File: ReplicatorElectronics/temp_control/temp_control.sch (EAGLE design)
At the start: 4 parts, among them Q1 IRL640A

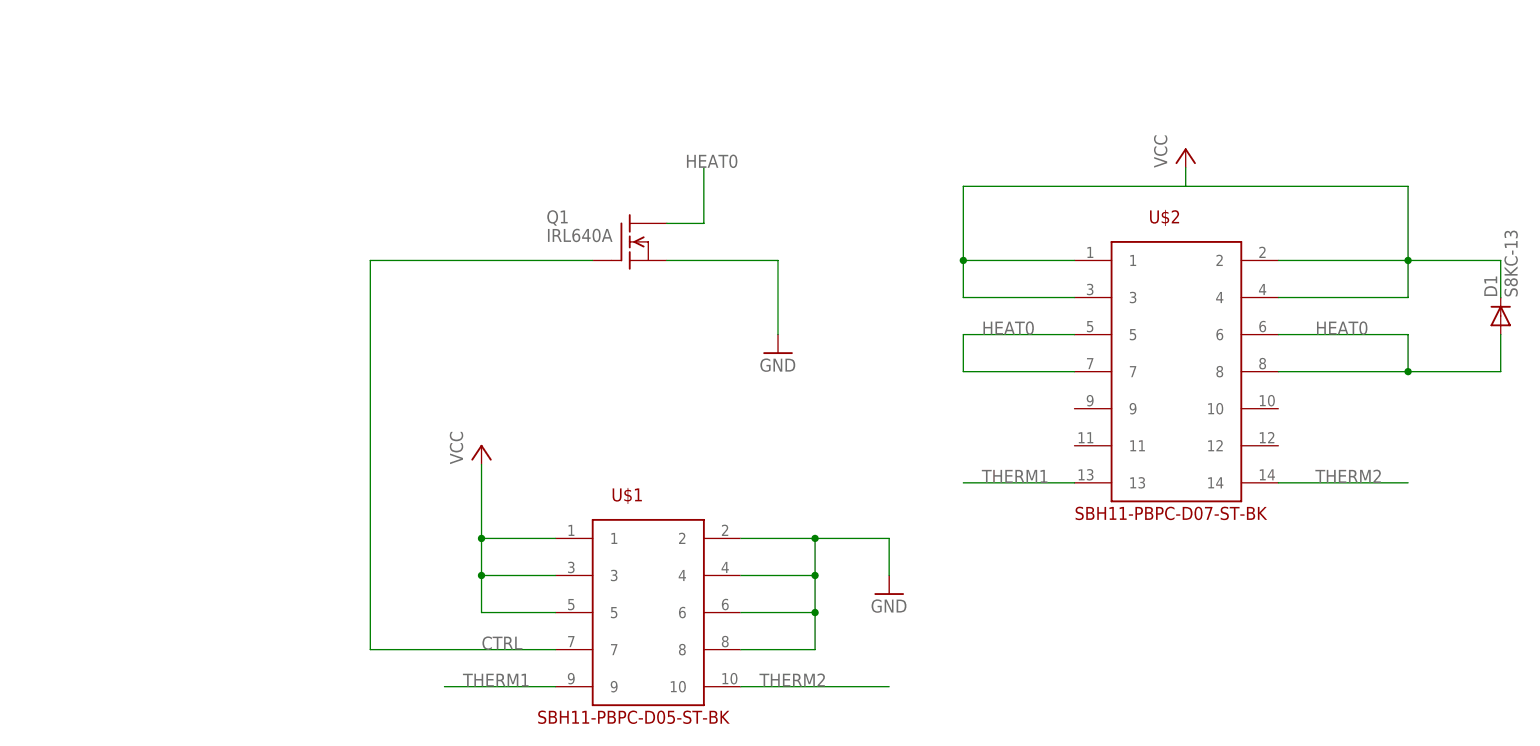
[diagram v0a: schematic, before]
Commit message: 3/17/12: Rev. 02 Temp Control Board. Replaced 2x7 rectangular header with 0.100" pitch screw terminal, added high-side totem pole driver for MOSFET, added clearance holes for mounting screws. Swapped diode D1 for slightly smaller part.
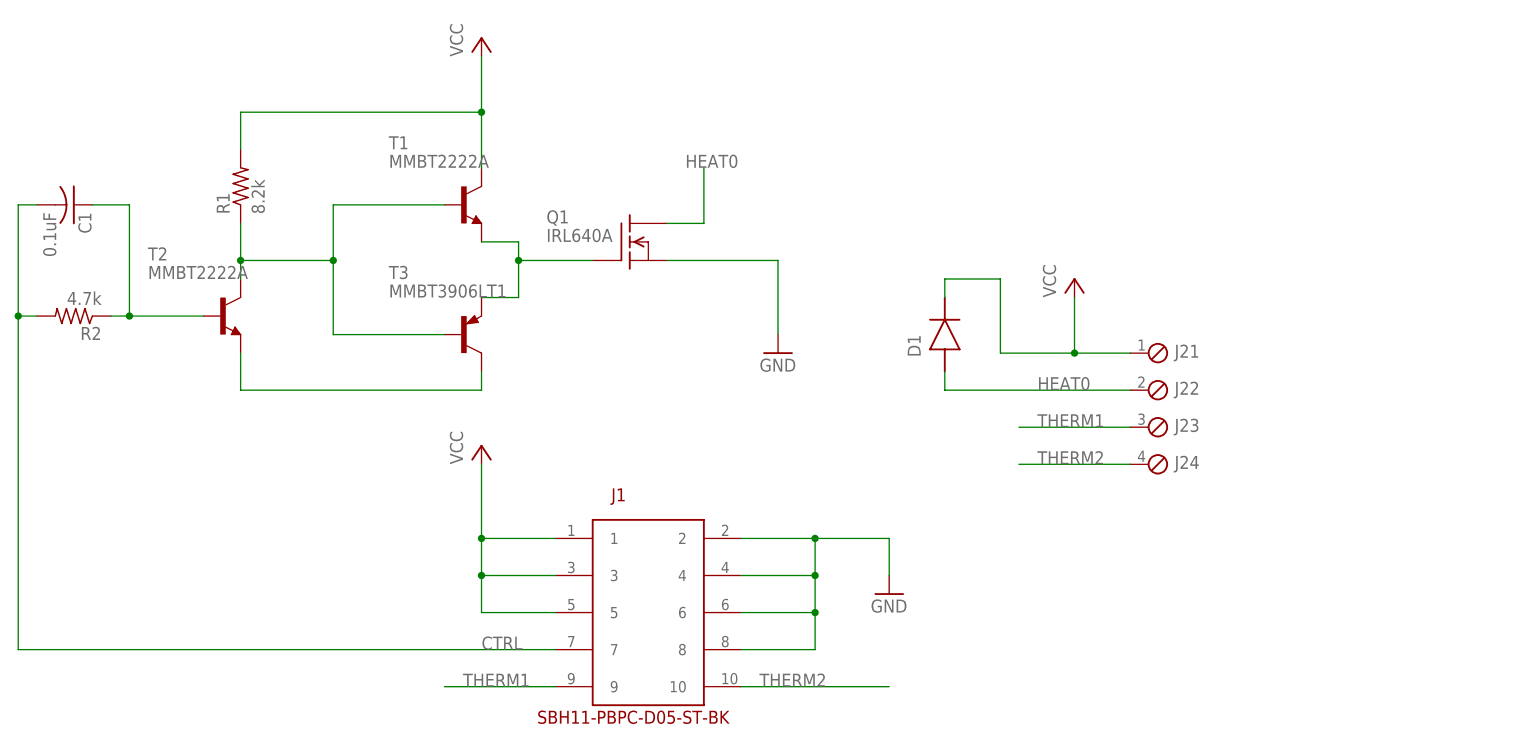
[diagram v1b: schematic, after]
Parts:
- removed U$2: SBH11-PBPC-D07-ST-BK, SBH11-PBPC-D07-ST-BK:SBH11-PBPC-D07-ST-BK
- added C1: 0.1uF, resistor:C-USC0603
- added J2: OSTVN04A150, con-OST-254:OSTVN04A150
- added R1: 8.2k, resistor:R-US_R0603
- added R2: 4.7k, resistor:R-US_R0603
- added T1, T2: MMBT2222A, transistor:MMBT2222ALT1-NPN-SOT23-BEC
- added T3: MMBT3906LT1, transistor:MMBT3906LT1-PNP-SOT23-BEC
- D1: value S8KC-13 -> B340A-13-F; device diode:DIODE-SMC -> chipKIT_Max32:DISCRETE_DIODESMA
- renumbered U$1 to J1
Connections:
- new net N$3: C1.1, R2.1, T2.B
- new net N$4: R1.1, T1.B, T2.C, T3.B
- new net N$6: Q1.G, T1.E, T3.E
- new net N$8: T2.E, T3.C
- net CTRL: now also C1.2, R2.2; no longer Q1.G
- net HEAT0: now also J22.1; no longer U$2.5, U$2.6, U$2.7, U$2.8
- net THERM1: now also J23.1; no longer U$2.13
- net THERM2: now also J24.1; no longer U$2.14
- net VCC: now also J21.1, R1.2, T1.C; no longer U$2.1, U$2.2, U$2.3, U$2.4

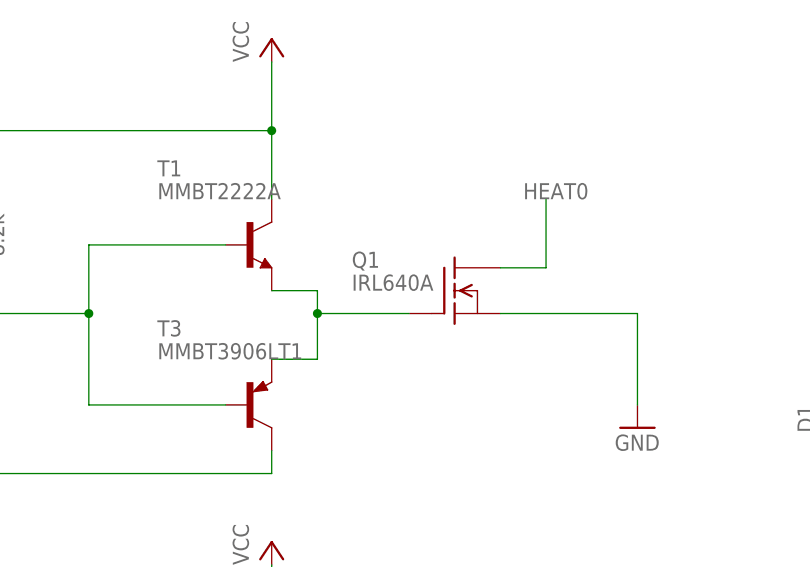
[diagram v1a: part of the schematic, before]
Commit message: 3/31/12: Rev. 3 of temp control board. Modified 2x5 header symbol, generated DXF files (one with holes only, another with holes and high-profile parts).
~ 0.5 hrs invested.
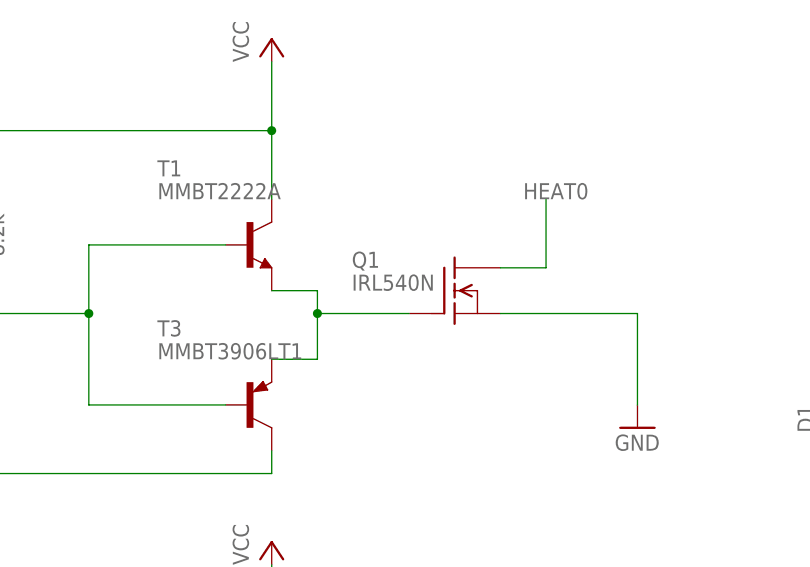
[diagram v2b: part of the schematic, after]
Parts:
- Q1: value IRL640A -> IRL540N
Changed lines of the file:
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@@
 </classes>
 <parts>
-<part name="Q1" library="transistor-fet" deviceset="SUP75N06-08" device="" value="IRL640A"/>
-<part name="J1" library="SBH11-PBPC-D05-ST-BK" deviceset="SBH11-PBPC-D05-ST-BK" device=""/>
+<part name="Q1" library="transistor-fet" deviceset="SUP75N06-08" device="" value="IRL540N"/>
 <part name="P+1" library="supply1" deviceset="VCC" device=""/>
 <part name="GND1" library="supply1" deviceset="GND" device=""/>
@@
 <part name="FRAME1" library="frames" deviceset="FRAME_C_L" device=""/>
 <part name="D1" library="chipKIT_Max32" deviceset="DISCRETE_DIODE" device="SMA" value="B340A-13-F"/>
+<part name="J1" library="SBH11-PBPC-D05-ST-BK" deviceset="SBH11-PBPC-D05-ST-BK" device=""/>
 </parts>
 <sheets>
@@
 <instances>
 <instance part="Q1" gate="G$1" x="22.86" y="73.66"/>
-<instance part="J1" gate="G$1" x="22.86" y="22.86"/>
 <instance part="P+1" gate="VCC" x="2.54" y="45.72"/>
 <instance part="GND1" gate="1" x="58.42" y="25.4"/>
@@
 <instance part="FRAME1" gate="G$2" x="200.66" y="-160.02"/>
 <instance part="D1" gate="G$1" x="66.04" y="60.96" rot="R270"/>
+<instance part="J1" gate="G$1" x="22.86" y="22.86"/>
 </instances>
 <busses>
@@
 <net name="VCC" class="0">
 <segment>
-<pinref part="J1" gate="G$1" pin="5"/>
 <wire x1="12.7" y1="22.86" x2="2.54" y2="22.86" width="0.1524" layer="91"/>
 <wire x1="2.54" y1="22.86" x2="2.54" y2="27.94" width="0.1524" layer="91"/>
-<pinref part="J1" gate="G$1" pin="3"/>
 <wire x1="2.54" y1="27.94" x2="12.7" y2="27.94" width="0.1524" layer="91"/>
 <wire x1="2.54" y1="27.94" x2="2.54" y2="33.02" width="0.1524" layer="91"/>
 <junction x="2.54" y="27.94"/>
-<pinref part="J1" gate="G$1" pin="1"/>
 <wire x1="2.54" y1="33.02" x2="12.7" y2="33.02" width="0.1524" layer="91"/>
 <wire x1="2.54" y1="33.02" x2="2.54" y2="43.18" width="0.1524" layer="91"/>
 <junction x="2.54" y="33.02"/>
 <pinref part="P+1" gate="VCC" pin="VCC"/>
+<pinref part="J1" gate="G$1" pin="1"/>
+<pinref part="J1" gate="G$1" pin="3"/>
+<pinref part="J1" gate="G$1" pin="5"/>
 </segment>
 <segment>
@@
 <net name="GND" class="0">
 <segment>
-<pinref part="J1" gate="G$1" pin="2"/>
 <wire x1="38.1" y1="33.02" x2="48.26" y2="33.02" width="0.1524" layer="91"/>
 <wire x1="48.26" y1="33.02" x2="58.42" y2="33.02" width="0.1524" layer="91"/>
 <wire x1="58.42" y1="33.02" x2="58.42" y2="27.94" width="0.1524" layer="91"/>
-<pinref part="J1" gate="G$1" pin="4"/>
 <wire x1="38.1" y1="27.94" x2="48.26" y2="27.94" width="0.1524" layer="91"/>
 <wire x1="48.26" y1="27.94" x2="48.26" y2="33.02" width="0.1524" layer="91"/>
 <junction x="48.26" y="33.02"/>
-<pinref part="J1" gate="G$1" pin="6"/>
 <wire x1="38.1" y1="22.86" x2="48.26" y2="22.86" width="0.1524" layer="91"/>
 <wire x1="48.26" y1="22.86" x2="48.26" y2="27.94" width="0.1524" layer="91"/>
 <junction x="48.26" y="27.94"/>
 <pinref part="GND1" gate="1" pin="GND"/>
-<pinref part="J1" gate="G$1" pin="8"/>
 <wire x1="38.1" y1="17.78" x2="48.26" y2="17.78" width="0.1524" layer="91"/>
 <wire x1="48.26" y1="17.78" x2="48.26" y2="22.86" width="0.1524" layer="91"/>
 <junction x="48.26" y="22.86"/>
+<pinref part="J1" gate="G$1" pin="2"/>
+<pinref part="J1" gate="G$1" pin="4"/>
+<pinref part="J1" gate="G$1" pin="6"/>
+<pinref part="J1" gate="G$1" pin="8"/>
 </segment>
 <segment>
@@
 <net name="THERM1" class="0">
 <segment>
-<pinref part="J1" gate="G$1" pin="9"/>
 <wire x1="12.7" y1="12.7" x2="-2.54" y2="12.7" width="0.1524" layer="91"/>
 <label x="0" y="12.7" size="1.778" layer="95"/>
+<pinref part="J1" gate="G$1" pin="9"/>
 </segment>
 <segment>
@@
 <net name="THERM2" class="0">
 <segment>
-<pinref part="J1" gate="G$1" pin="10"/>
 <wire x1="38.1" y1="12.7" x2="58.42" y2="12.7" width="0.1524" layer="91"/>
 <label x="40.64" y="12.7" size="1.778" layer="95"/>
+<pinref part="J1" gate="G$1" pin="10"/>
 </segment>
 <segment>
@@
 <net name="CTRL" class="0">
 <segment>
-<pinref part="J1" gate="G$1" pin="7"/>
 <label x="2.54" y="17.78" size="1.778" layer="95"/>
 <pinref part="C1" gate="G$1" pin="2"/>
@@
 <wire x1="-60.96" y1="17.78" x2="-60.96" y2="63.5" width="0.1524" layer="91"/>
 <junction x="-60.96" y="63.5"/>
+<pinref part="J1" gate="G$1" pin="7"/>
 </segment>
 </net>
